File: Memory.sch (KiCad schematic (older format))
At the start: 20 parts, among them U10 DRAM_4464, U11 DRAM_4464, U12 DRAM_4464, U34 MMMU, U9 DRAM_4464

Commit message: Tracking
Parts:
- added J50, J51: Conn_01x02, Connector_PinHeader_2.54mm:PinHeader_1x02_P2.54mm_Vertical, symbol Connector_Generic:Conn_01x02
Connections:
- net GND: now also J50.1 (Pin_1), J50.2 (Pin_2), J51.1 (Pin_1), J51.2 (Pin_2)
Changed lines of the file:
@@
 Wire Wire Line
 	7575 4250 6025 4250
+$Comp
+L power:GND #PWR0250
+U 1 1 6032EFD4
+P 950 5125
+F 0 "#PWR0250" H 950 4875 50  0001 C CNN
+F 1 "GND" H 955 4952 50  0000 C CNN
+F 2 "" H 950 5125 50  0001 C CNN
+F 3 "" H 950 5125 50  0001 C CNN
+	1    950  5125
+	1    0    0    -1
+$EndComp
+Connection ~ 950  4900
+Wire Wire Line
+	950  4900 950  5125
+Wire Wire Line
+	950  4800 950  4900
+$Comp
+L Connector_Generic:Conn_01x02 J50
+U 1 1 6032DAF0
+P 1150 4800
+F 0 "J50" H 1230 4792 50  0000 L CNN
+F 1 "Conn_01x02" H 1230 4701 50  0000 L CNN
+F 2 "Connector_PinHeader_2.54mm:PinHeader_1x02_P2.54mm_Vertical" H 1150 4800 50  0001 C CNN
+F 3 "~" H 1150 4800 50  0001 C CNN
+	1    1150 4800
+	1    0    0    -1
+$EndComp
+$Comp
+L Connector_Generic:Conn_01x02 J51
+U 1 1 60336F5B
+P 1150 5525
+F 0 "J51" H 1230 5517 50  0000 L CNN
+F 1 "Conn_01x02" H 1230 5426 50  0000 L CNN
+F 2 "Connector_PinHeader_2.54mm:PinHeader_1x02_P2.54mm_Vertical" H 1150 5525 50  0001 C CNN
+F 3 "~" H 1150 5525 50  0001 C CNN
+	1    1150 5525
+	1    0    0    -1
+$EndComp
+$Comp
+L power:GND #PWR0251
+U 1 1 60337497
+P 950 5800
+F 0 "#PWR0251" H 950 5550 50  0001 C CNN
+F 1 "GND" H 955 5627 50  0000 C CNN
+F 2 "" H 950 5800 50  0001 C CNN
+F 3 "" H 950 5800 50  0001 C CNN
+	1    950  5800
+	1    0    0    -1
+$EndComp
+Wire Wire Line
+	950  5625 950  5800
+Wire Wire Line
+	950  5525 950  5625
+Connection ~ 950  5625
 $EndSCHEMATC

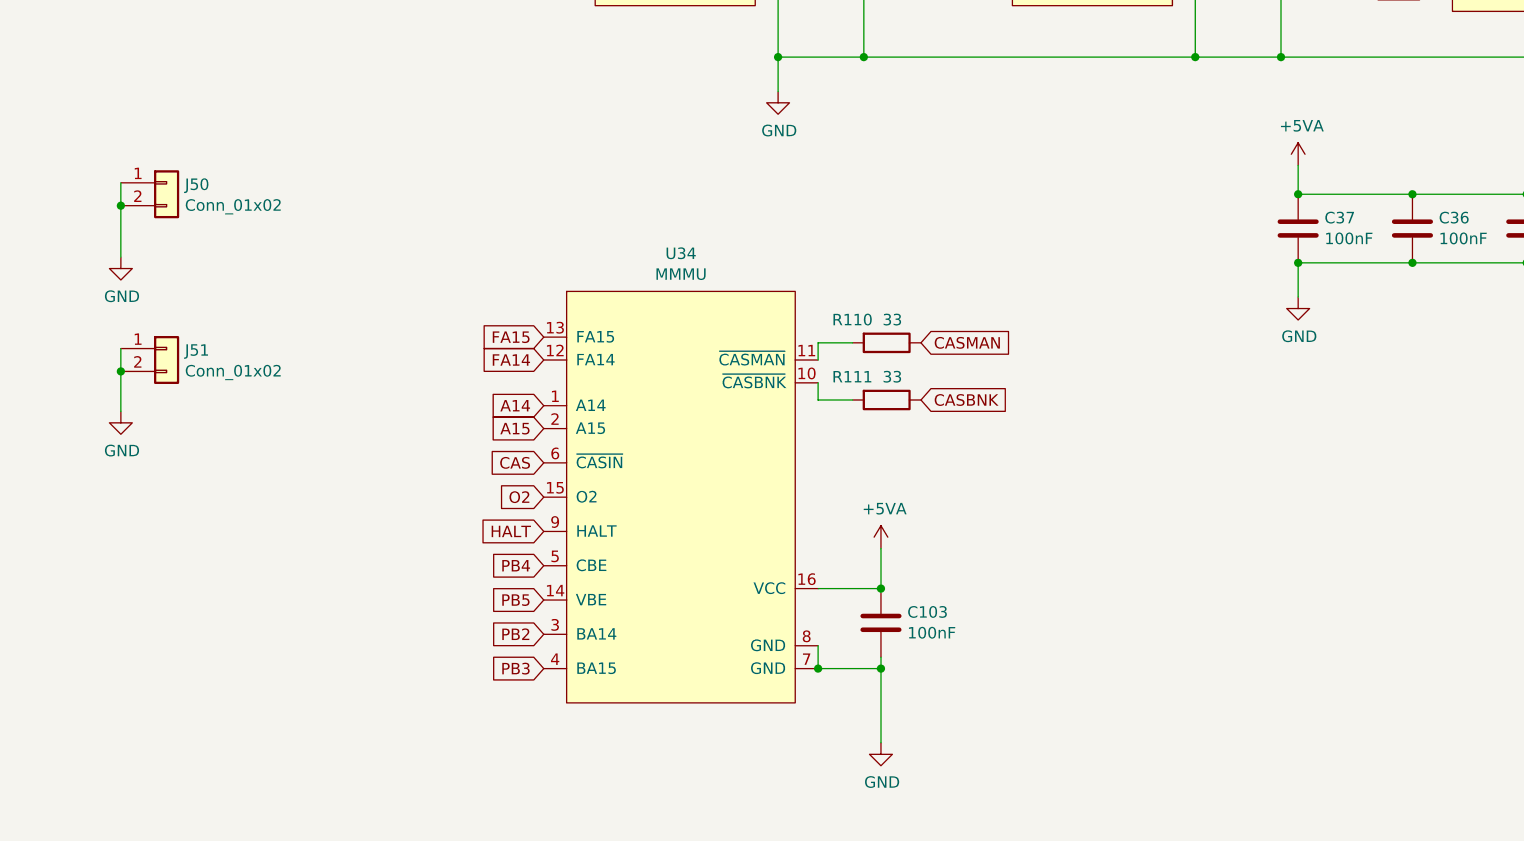
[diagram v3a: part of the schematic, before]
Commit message: Add 74LS95
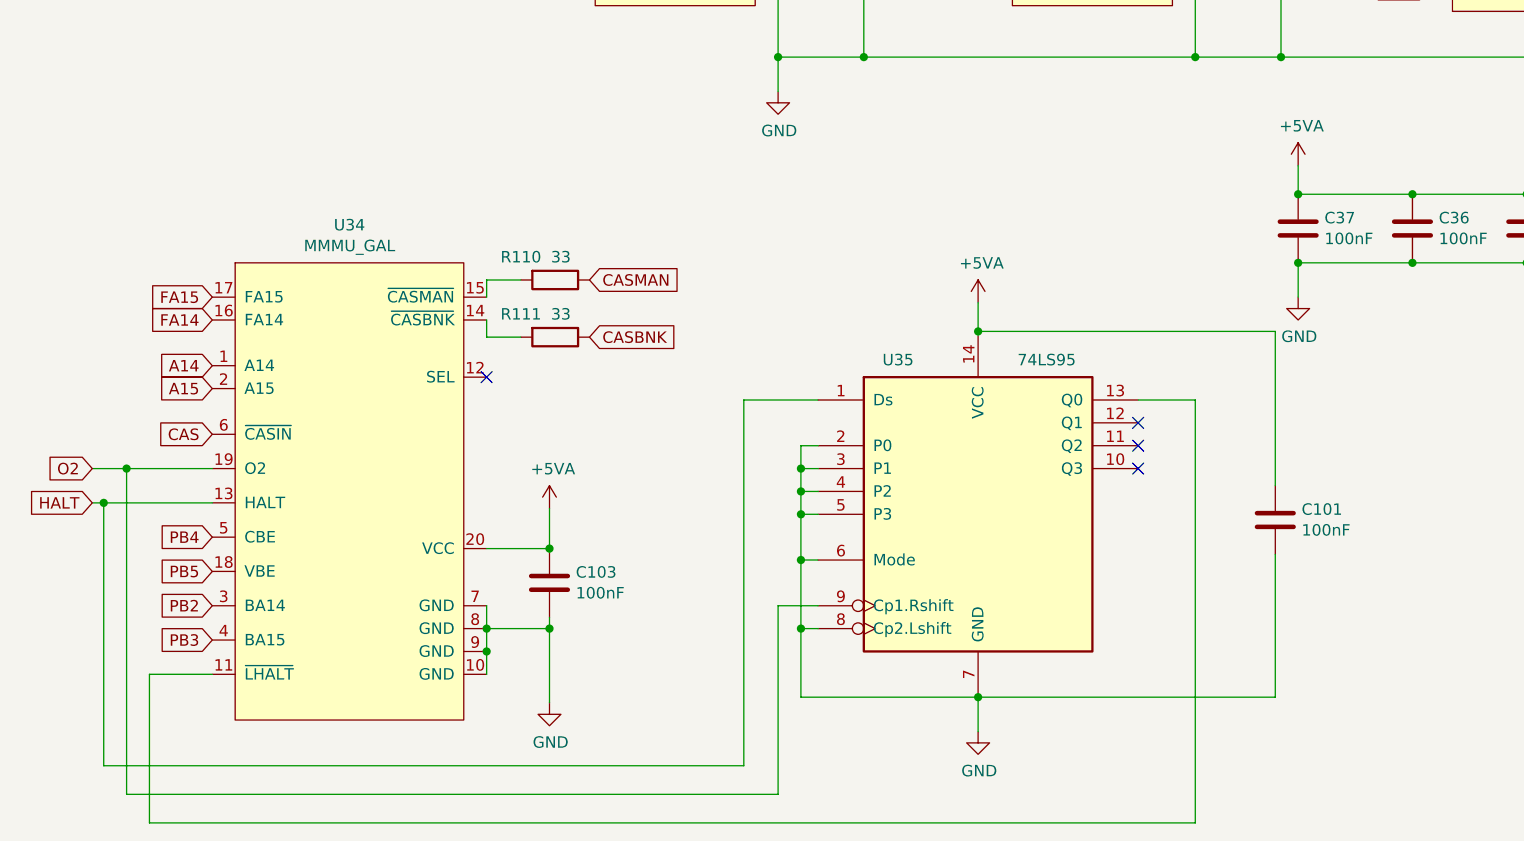
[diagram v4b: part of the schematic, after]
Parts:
- removed J50, J51: Conn_01x02, Connector_PinHeader_2.54mm:PinHeader_1x02_P2.54mm_Vertical, symbol Connector_Generic:Conn_01x02
- removed U34: MMMU, Package_DIP:DIP-16_W7.62mm_Socket, symbol Atari:MMMU
- added C101: 100nF, Atari:C_Axial_L5.1mm_D2.5mm_P12.50mm_Horizontal, symbol Device:C
- added U34: MMMU_GAL, Package_DIP:DIP-20_W7.62mm_Socket, symbol Atari:MMMU_GAL
- added U35: 74LS95, Package_DIP:DIP-14_W7.62mm_Socket, symbol 74xx:74LS95
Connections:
- net +5VA: now also C101.1, U34.20 (VCC), U35.14 (VCC)
- net A14: now also U34.1 (A14)
- net A15: now also U34.2 (A15)
- net CAS: now also U34.6 (~CASIN)
- net FA14: now also U34.16 (FA14)
- net FA15: now also U34.17 (FA15)
- net GND: now also C101.2, U34.10 (GND), U34.7 (GND), U34.8 (GND), U34.9 (GND), U35.2 (P0), U35.3 (P1), U35.4 (P2), U35.5 (P3), U35.6 (Mode), U35.7 (GND), U35.8 (Cp2.Lshift)
- net HALT: now also U34.13 (HALT), U35.1 (Ds)
- net O2: now also U34.19 (O2), U35.9 (Cp1.Rshift)
- net PB2: now also U34.3 (BA14)
- net PB3: now also U34.4 (BA15)
- net PB4: now also U34.5 (CBE)
- net PB5: now also U34.18 (VBE)
- net at R111.2: now also U34.14 (~CASBNK)
- net at R110.2: now also U34.15 (~CASMAN)
- new net: U34.11 (~LHALT), U35.13 (Q0)
- no-connect marks 0 -> 4
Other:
- moved on the sheet: C103, R110, R111
